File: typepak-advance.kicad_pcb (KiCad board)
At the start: 2 copper layers, 51.7 x 32 mm, 24 parts, among them J2 Conn_01x04, J3 Conn_01x02, J5 Conn_01x32_Pin, J6 Conn_01x10, Q1 AO3407, Q2 AO3407, U1 E73-2G4M08S1C, U2 AP2112K-3.3, U3 TP4054

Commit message: Initial Commit.
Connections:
- J5 pad 16: P0.28 -> P1.02
- J5 pad 17: P1.02 -> P0.17
- J5 pad 18: P1.04 -> P0.22
- J5 pad 23: P0.17 -> P0.28
- J5 pad 25: P0.22 -> P1.04
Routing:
- net P1.04: track 30.6 -> 42.0 mm, vias 0 -> 2
- net P0.28: track 33.7 -> 44.7 mm, vias 1 -> 2
- net P0.22: track 37.9 -> 28.8 mm, vias 1 -> 0
- net P0.17: track 32.9 -> 25.0 mm, vias 1 -> 0
- net P1.02: track 30.0 -> 33.3 mm, vias 0 -> 2
- net P1.06: track 31.3 -> 34.1 mm
- net P0.20: track 35.4 -> 36.4 mm
- net P1.00: track 40.3 -> 41.1 mm

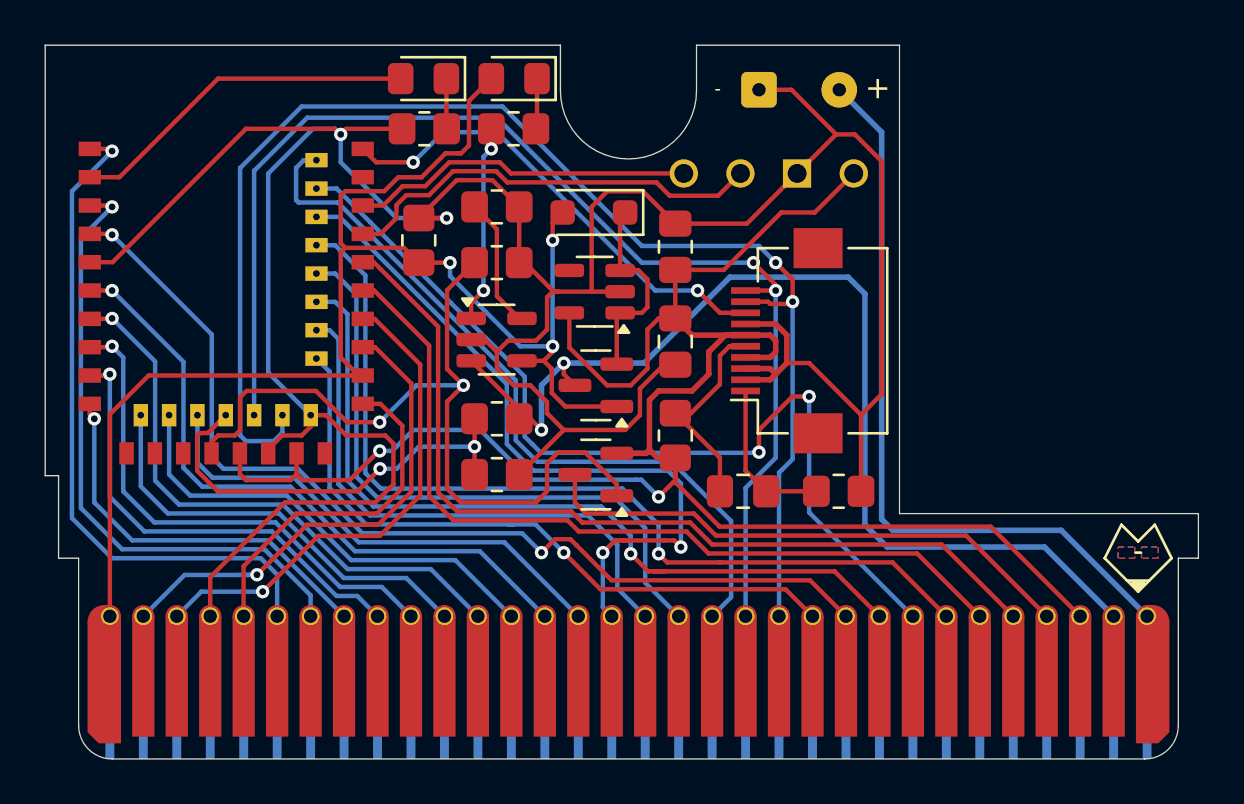
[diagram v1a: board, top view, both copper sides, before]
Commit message: Cleaned up traces.
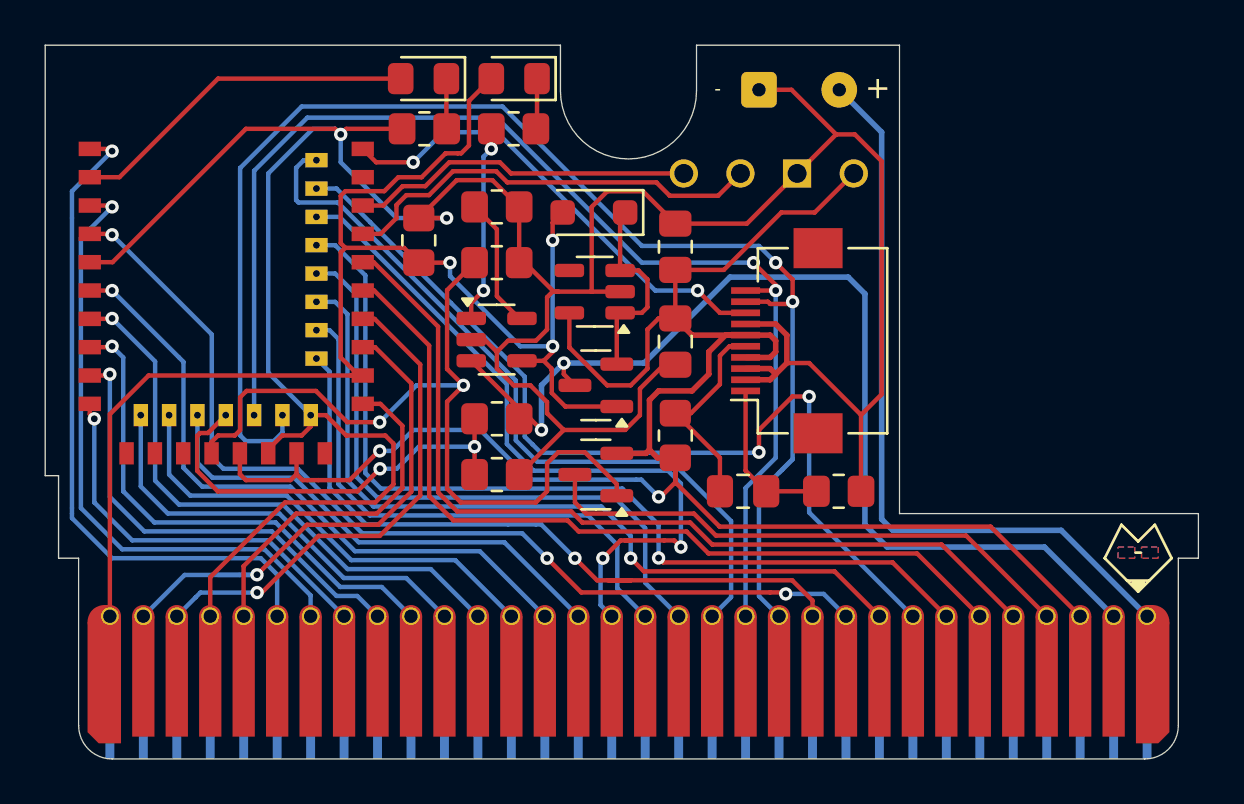
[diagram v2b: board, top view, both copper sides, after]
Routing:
- net P0.07: track 61.6 -> 63.2 mm
- net DATA-: track 22.3 -> 23.5 mm
- net P0.15: track 30.3 -> 31.5 mm
- net P1.02: track 33.3 -> 32.8 mm
- net P0.28: track 44.7 -> 44.2 mm, vias 2 -> 3

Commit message: Updated to hand-solder footprints.
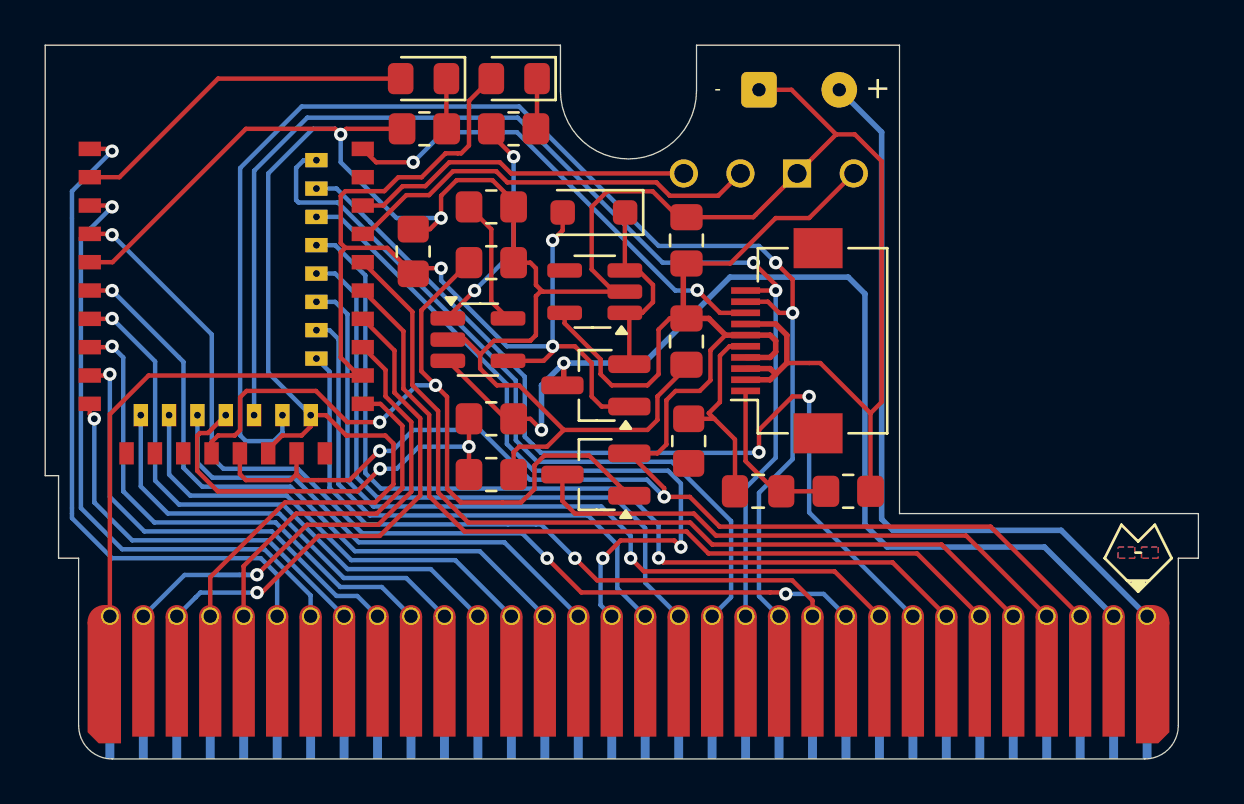
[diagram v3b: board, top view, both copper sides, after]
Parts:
- Q1, Q2: footprint Package_TO_SOT_SMD:SOT-23 -> Package_TO_SOT_SMD:SOT-23_Handsoldering
- U2, U3: footprint Package_TO_SOT_SMD:SOT-23-5 -> Package_TO_SOT_SMD:SOT-23-5_HandSoldering
- moved U3 0.84 mm to (94.4, 38.2)
- moved C2 0.68 mm to (107.0, 45.0)
- moved FB1 0.65 mm to (103.8, 42.8)
- moved C3 0.58 mm to (103.8, 33.8)
- moved R1 0.56 mm to (91.5, 34.2)
- moved C1 0.50 mm to (103.8, 38.3)
- moved FB2 0.42 mm to (111.0, 45.0)
- moved R5 0.25 mm to (95.0, 32.2)
- moved R6 0.25 mm to (95.0, 41.8)
- moved R7 0.25 mm to (95.0, 44.2)
- moved R9 0.25 mm to (95.0, 34.8)
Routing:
- net GND: track 146.8 -> 150.6 mm
- net VBUS: track 65.1 -> 66.6 mm
- net Net-(U3-STAT): track 8.97 -> 10.1 mm
- net P0.15: track 31.5 -> 30.5 mm
- net POWER_PIN: track 36.8 -> 35.8 mm
- net nRF_VDD: track 86.5 -> 85.7 mm
- net Net-(J6-Pin_6): track 10.1 -> 9.30 mm
- net P0.07: track 63.2 -> 62.5 mm
- net VBAT: track 47.9 -> 48.5 mm
- net EXT_VCC: track 24.5 -> 25.0 mm
